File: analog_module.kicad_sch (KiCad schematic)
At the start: 9 parts, among them U42 ADS1115

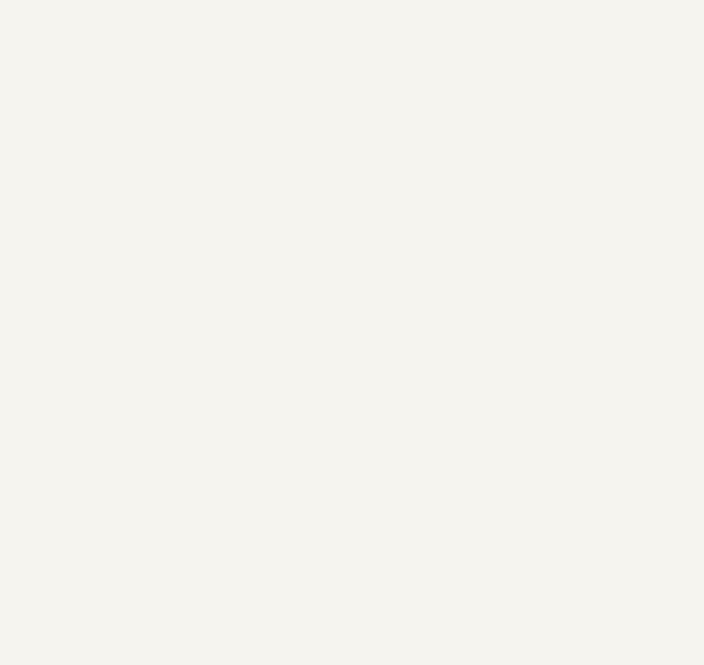
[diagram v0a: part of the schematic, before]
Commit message: power part designed
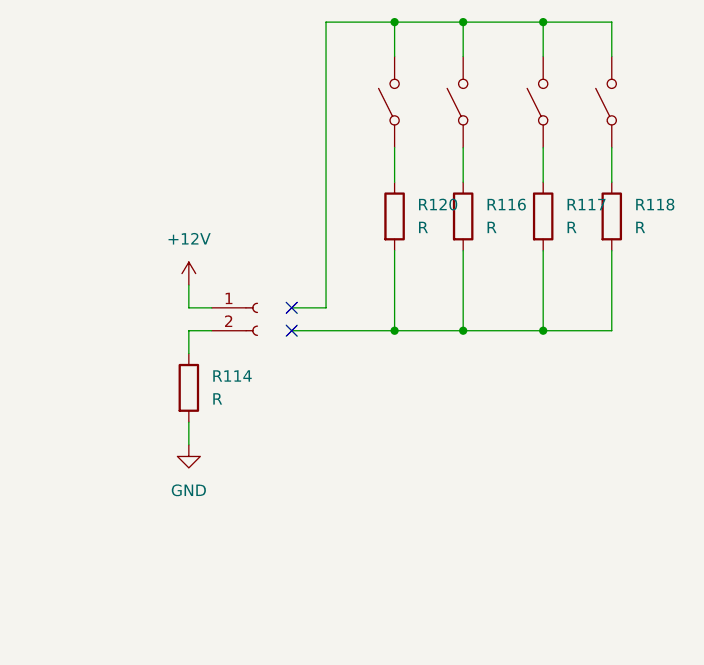
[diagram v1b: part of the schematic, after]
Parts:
- added J20: Conn_01x02_Female, symbol Connector:Conn_01x02_Female
- added R114, R116, R117, R118, R120: R, symbol Device:R
- added SW10, SW11, SW8, SW9: SW_SPST, symbol Switch:SW_SPST
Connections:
- net GND: now also R114.2
- new net: J20.2 (Pin_2), R114.1
- new net: R120.1, SW8.1 (A)
- new net: SW10.2 (B), SW11.2 (B), SW8.2 (B), SW9.2 (B)
- new net: R116.2, R117.2, R118.2, R120.2
- new net: R117.1, SW10.1 (A)
- new net: R116.1, SW9.1 (A)
- new net: R118.1, SW11.1 (A)
- new net +12V: J20.1 (Pin_1)
- no-connect marks 0 -> 2

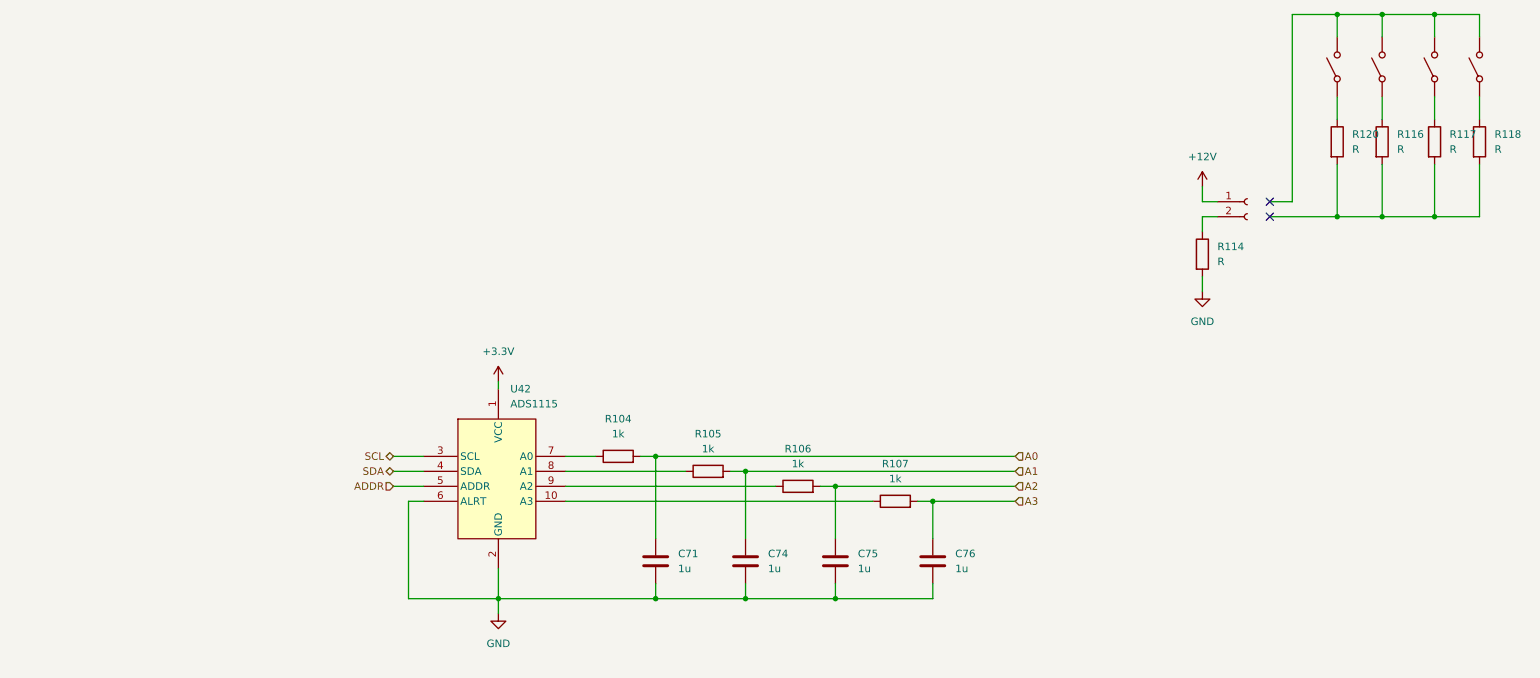
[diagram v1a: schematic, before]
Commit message: ADC resistors and outputs added
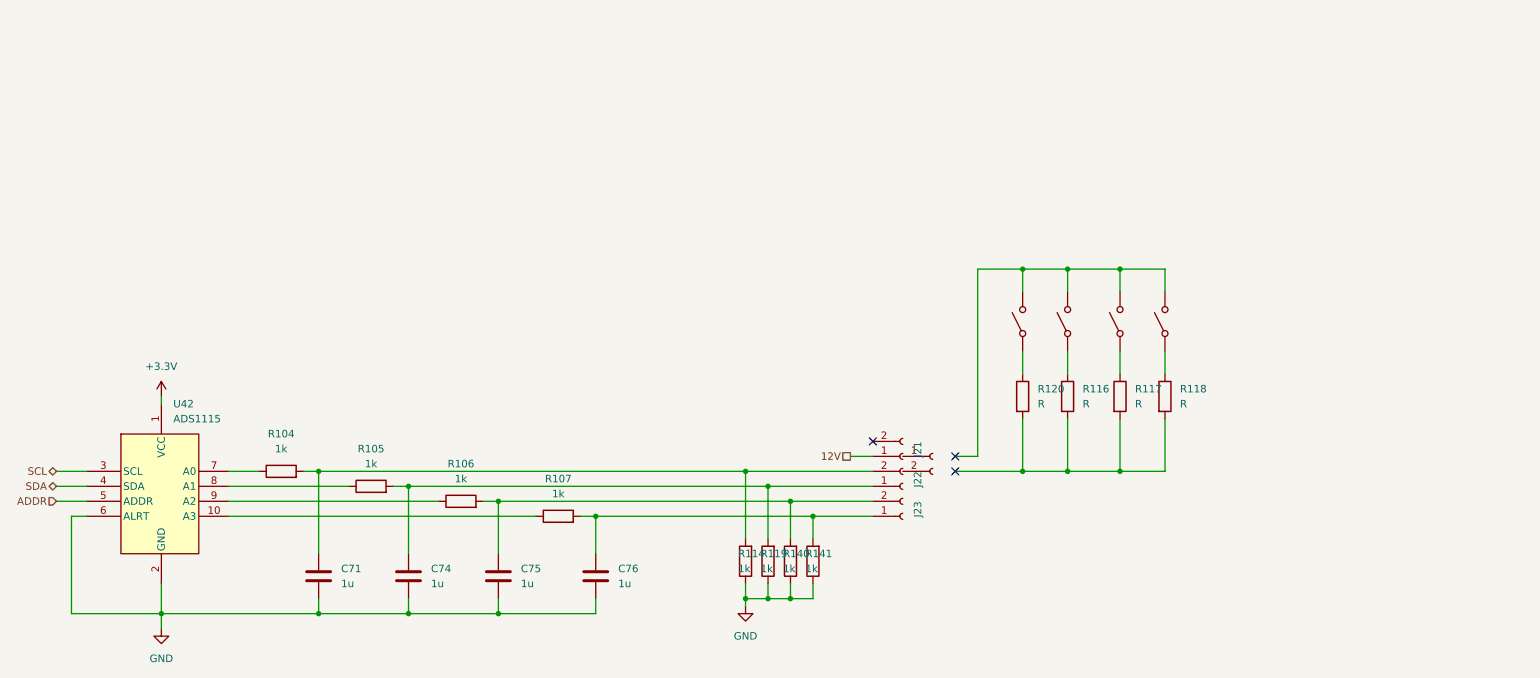
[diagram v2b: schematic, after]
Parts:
- added J21, J22, J23: Conn_01x02_Female, TerminalBlock_Phoenix:TerminalBlock_Phoenix_MKDS-1,5-2_1x02_P5.00mm_Horizontal, symbol Connector:Conn_01x02_Female
- added R119, R140, R141: 1k, Resistor_THT:R_Axial_DIN0204_L3.6mm_D1.6mm_P7.62mm_Horizontal, symbol Device:R
- R114: value R -> 1k; footprint (none) -> Resistor_THT:R_Axial_DIN0204_L3.6mm_D1.6mm_P7.62mm_Horizontal; now in the parts list
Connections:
- net GND: now also R114.1, R119.1, R140.1, R141.1; no longer R114.2
- net at J20.2 (Pin_2): no longer R114.1
- net +12V: no longer names the net of J20.1 (Pin_1)
- net A0: no longer names the net of C71.1, R104.2
- net A0: now also R114.2, J22.2 (Pin_2)
- net A1: no longer names the net of C74.1, R105.2
- net A1: now also J22.1 (Pin_1), R119.2
- net A2: no longer names the net of C75.1, R106.2
- net A2: now also J23.2 (Pin_2), R140.2
- net A3: no longer names the net of C76.1, R107.2
- net A3: now also J23.1 (Pin_1), R141.2
- new net 12V: J21.1 (Pin_1)
- no-connect marks 2 -> 3
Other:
- moved on the sheet: C71, C74, C75, C76, R104, R105, R106, R107, R116, R117, R118, R120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

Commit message: project finished before changes
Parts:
- renumbered J21 to J24, J22 to J25, J23 to J26, R116 to R121, R117 to R122, R118 to R123, R114 to R142, R119 to R143, R140 to R144, R141 to R145, SW8 to SW12, SW9 to SW13, SW10 to SW14, SW11 to SW15
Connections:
- net 12V: now also J24.2 (Pin_2)
- no-connect marks 3 -> 2
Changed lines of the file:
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@@
   (junction (at 161.29 96.52) (diameter 0) (color 0 0 0 0)
   )
-  (no_connect (at 175.26 86.36))
+  (junction (at 172.72 88.9) (diameter 0) (color 0 0 0 0)
+  )
   (no_connect (at 189.23 88.9))
   (no_connect (at 189.23 91.44))
@@
     (stroke (width 0) (type default) (color 0 0 0 0))
   )
+  (wire (pts (xy 172.72 86.36) (xy 172.72 88.9))
+    (stroke (width 0) (type default) (color 0 0 0 0))
+  )
   (wire (pts (xy 66.04 99.06) (xy 118.11 99.06))
     (stroke (width 0) (type default) (color 0 0 0 0))
@@
     (stroke (width 0) (type default) (color 0 0 0 0))
   )
+  (wire (pts (xy 172.72 88.9) (xy 175.26 88.9))
+    (stroke (width 0) (type default) (color 0 0 0 0))
+  )
   (wire (pts (xy 200.66 57.15) (xy 208.28 57.15))
     (stroke (width 0) (type default) (color 0 0 0 0))
@@
     (stroke (width 0) (type default) (color 0 0 0 0))
   )
-  (wire (pts (xy 171.45 88.9) (xy 175.26 88.9))
+  (wire (pts (xy 171.45 88.9) (xy 172.72 88.9))
     (stroke (width 0) (type default) (color 0 0 0 0))
   )
@@
   )
   (wire (pts (xy 54.61 78.74) (xy 54.61 80.01))
+    (stroke (width 0) (type default) (color 0 0 0 0))
+  )
+  (wire (pts (xy 175.26 86.36) (xy 172.72 86.36))
     (stroke (width 0) (type default) (color 0 0 0 0))
   )
@@
   (symbol (lib_id "Device:R") (at 153.67 106.68 180) (unit 1)
     (in_bom yes) (on_board yes)
-    (property "Reference" "R114" (id 0) (at 152.4 105.41 0)
+    (property "Reference" "R142" (id 0) (at 152.4 105.41 0)
       (effects (font (size 1.27 1.27)) (justify right))
     )
@@
   (symbol (lib_id "Device:R") (at 165.1 106.68 180) (unit 1)
     (in_bom yes) (on_board yes)
-    (property "Reference" "R141" (id 0) (at 163.83 105.41 0)
+    (property "Reference" "R145" (id 0) (at 163.83 105.41 0)
       (effects (font (size 1.27 1.27)) (justify right))
     )
@@
   (symbol (lib_id "Switch:SW_SPST") (at 200.66 66.04 90) (unit 1)
     (in_bom no) (on_board no) (fields_autoplaced)
-    (property "Reference" "SW8" (id 0) (at 201.93 64.7699 90)
+    (property "Reference" "SW12" (id 0) (at 201.93 64.7699 90)
       (effects (font (size 1.27 1.27)) (justify right) hide)
     )
@@
   (symbol (lib_id "Connector:Conn_01x02_Female") (at 180.34 99.06 0) (mirror x) (unit 1)
     (in_bom yes) (on_board yes)
-    (property "Reference" "J23" (id 0) (at 182.88 96.52 90)
+    (property "Reference" "J26" (id 0) (at 182.88 96.52 90)
       (effects (font (size 1.27 1.27)) (justify left))
     )
@@
   (symbol (lib_id "Device:R") (at 217.17 78.74 0) (unit 1)
     (in_bom no) (on_board no) (fields_autoplaced)
-    (property "Reference" "R117" (id 0) (at 219.71 77.4699 0)
+    (property "Reference" "R122" (id 0) (at 219.71 77.4699 0)
       (effects (font (size 1.27 1.27)) (justify left))
     )
@@
   (symbol (lib_id "Connector:Conn_01x02_Female") (at 180.34 93.98 0) (mirror x) (unit 1)
     (in_bom yes) (on_board yes)
-    (property "Reference" "J22" (id 0) (at 182.88 91.44 90)
+    (property "Reference" "J25" (id 0) (at 182.88 91.44 90)
       (effects (font (size 1.27 1.27)) (justify left))
     )
@@
   (symbol (lib_id "power:GND") (at 153.67 114.3 0) (unit 1)
     (in_bom yes) (on_board yes) (fields_autoplaced)
-    (property "Reference" "#PWR0131" (id 0) (at 153.67 120.65 0)
+    (property "Reference" "#PWR0150" (id 0) (at 153.67 120.65 0)
       (effects (font (size 1.27 1.27)) hide)
     )
@@
   (symbol (lib_id "Device:R") (at 161.29 106.68 180) (unit 1)
     (in_bom yes) (on_board yes)
-    (property "Reference" "R140" (id 0) (at 160.02 105.41 0)
+    (property "Reference" "R144" (id 0) (at 160.02 105.41 0)
       (effects (font (size 1.27 1.27)) (justify right))
     )
@@
   (symbol (lib_id "Device:R") (at 208.28 78.74 0) (unit 1)
     (in_bom no) (on_board no) (fields_autoplaced)
-    (property "Reference" "R116" (id 0) (at 210.82 77.4699 0)
+    (property "Reference" "R121" (id 0) (at 210.82 77.4699 0)
       (effects (font (size 1.27 1.27)) (justify left))
     )
@@
   (symbol (lib_id "Device:R") (at 157.48 106.68 180) (unit 1)
     (in_bom yes) (on_board yes)
-    (property "Reference" "R119" (id 0) (at 156.21 105.41 0)
+    (property "Reference" "R143" (id 0) (at 156.21 105.41 0)
       (effects (font (size 1.27 1.27)) (justify right))
     )
@@
   (symbol (lib_id "Switch:SW_SPST") (at 208.28 66.04 90) (unit 1)
     (in_bom no) (on_board no) (fields_autoplaced)
-    (property "Reference" "SW9" (id 0) (at 209.55 64.7699 90)
+    (property "Reference" "SW13" (id 0) (at 209.55 64.7699 90)
       (effects (font (size 1.27 1.27)) (justify right) hide)
     )
@@
   (symbol (lib_id "Connector:Conn_01x02_Female") (at 180.34 88.9 0) (mirror x) (unit 1)
     (in_bom yes) (on_board yes)
-    (property "Reference" "J21" (id 0) (at 182.88 86.36 90)
+    (property "Reference" "J24" (id 0) (at 182.88 86.36 90)
       (effects (font (size 1.27 1.27)) (justify left))
     )
@@
   (symbol (lib_id "Switch:SW_SPST") (at 217.17 66.04 90) (unit 1)
     (in_bom no) (on_board no) (fields_autoplaced)
-    (property "Reference" "SW10" (id 0) (at 218.44 64.7699 90)
+    (property "Reference" "SW14" (id 0) (at 218.44 64.7699 90)
       (effects (font (size 1.27 1.27)) (justify right) hide)
     )
@@
   (symbol (lib_id "Device:R") (at 224.79 78.74 0) (unit 1)
     (in_bom no) (on_board no) (fields_autoplaced)
-    (property "Reference" "R118" (id 0) (at 227.33 77.4699 0)
+    (property "Reference" "R123" (id 0) (at 227.33 77.4699 0)
       (effects (font (size 1.27 1.27)) (justify left))
     )
@@
   (symbol (lib_id "Switch:SW_SPST") (at 224.79 66.04 90) (unit 1)
     (in_bom no) (on_board no) (fields_autoplaced)
-    (property "Reference" "SW11" (id 0) (at 226.06 64.7699 90)
+    (property "Reference" "SW15" (id 0) (at 226.06 64.7699 90)
       (effects (font (size 1.27 1.27)) (justify right) hide)
     )

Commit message: v2.1 finished
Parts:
- R142, R143, R144, R145: footprint Resistor_THT:R_Axial_DIN0204_L3.6mm_D1.6mm_P7.62mm_Horizontal -> Resistor_SMD:R_0805_2012Metric_Pad1.20x1.40mm_HandSolder
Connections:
- no-connect marks 2 -> 4
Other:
- note added: "Analog switch"
- moved on the sheet: R120, R121, R122, R123

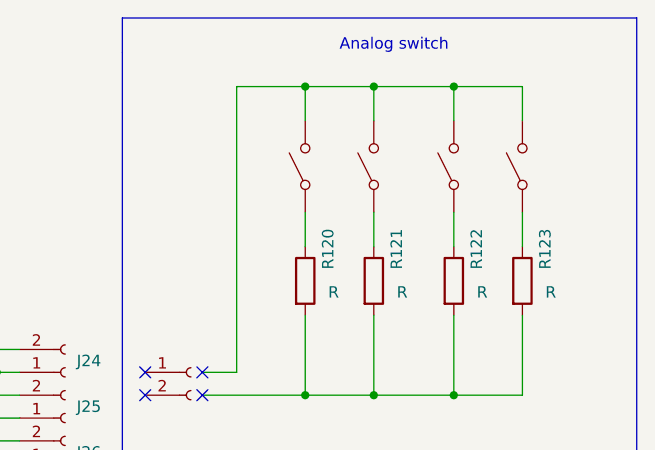
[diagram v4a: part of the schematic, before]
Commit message: updated footprints on board and sgematics
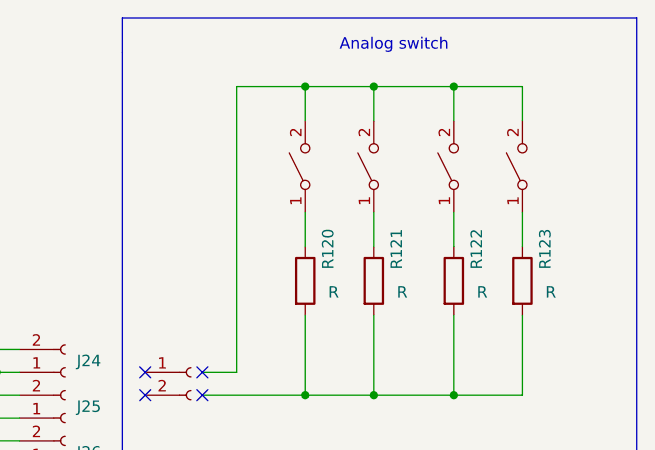
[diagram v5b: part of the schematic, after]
